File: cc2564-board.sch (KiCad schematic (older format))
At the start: 70 parts, among them J1 TYPE-C-31-M-12, J2 Conn_ARM_JTAG_SWD_10, J3 Conn_01x16, J4 Conn_01x16, J5 BOOT, J7 1909763-1, J8 Conn_01x04, SW1 SW_Push, U1 LD1117#33, U2 USBLC6-2P6, U3 LD1117#18, U4 STM32F103C8Tx, U5 TXB0104D, U6 TXB0104D, U7 CC2564CRVMR, Y1 ECS-80-18-30-JGN-TR, Y2 ECS-327MVATX-3-CN-TR, Y3 ECS-260-8-36CKM-TR

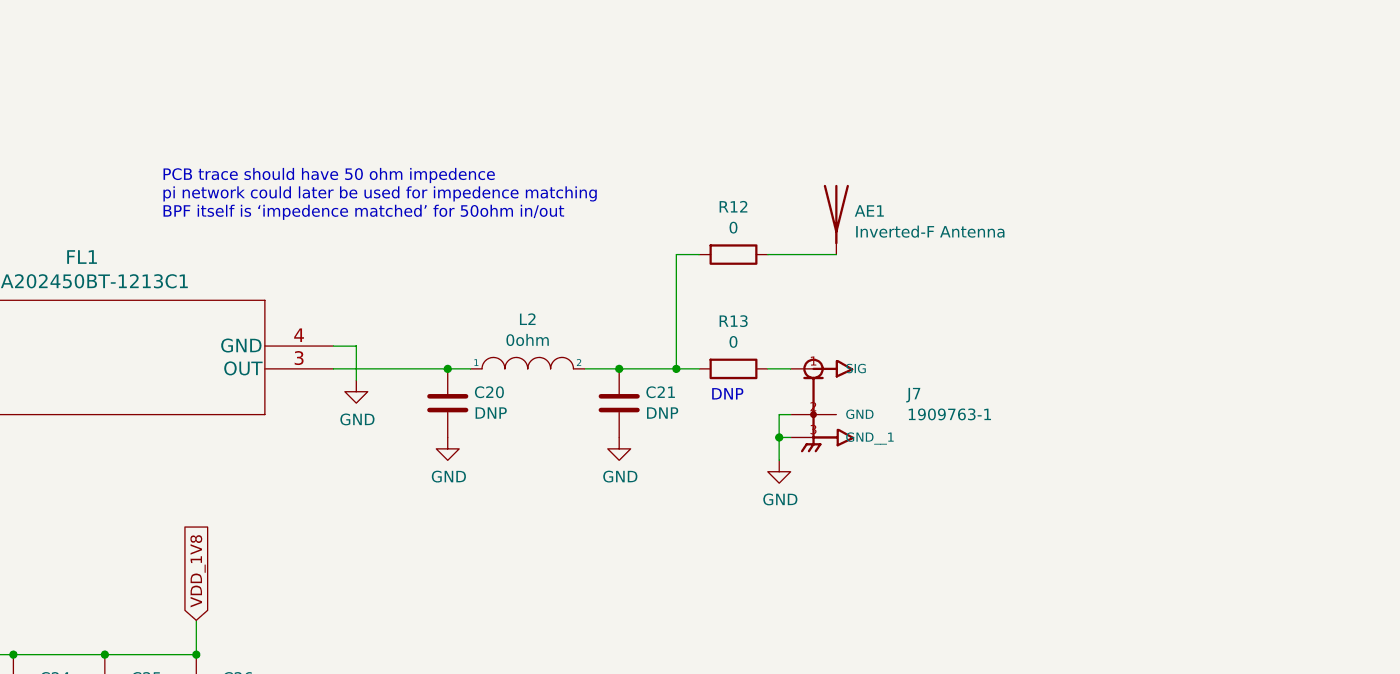
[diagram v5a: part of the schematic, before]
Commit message: Use meandered PIFA from TI app note AN043
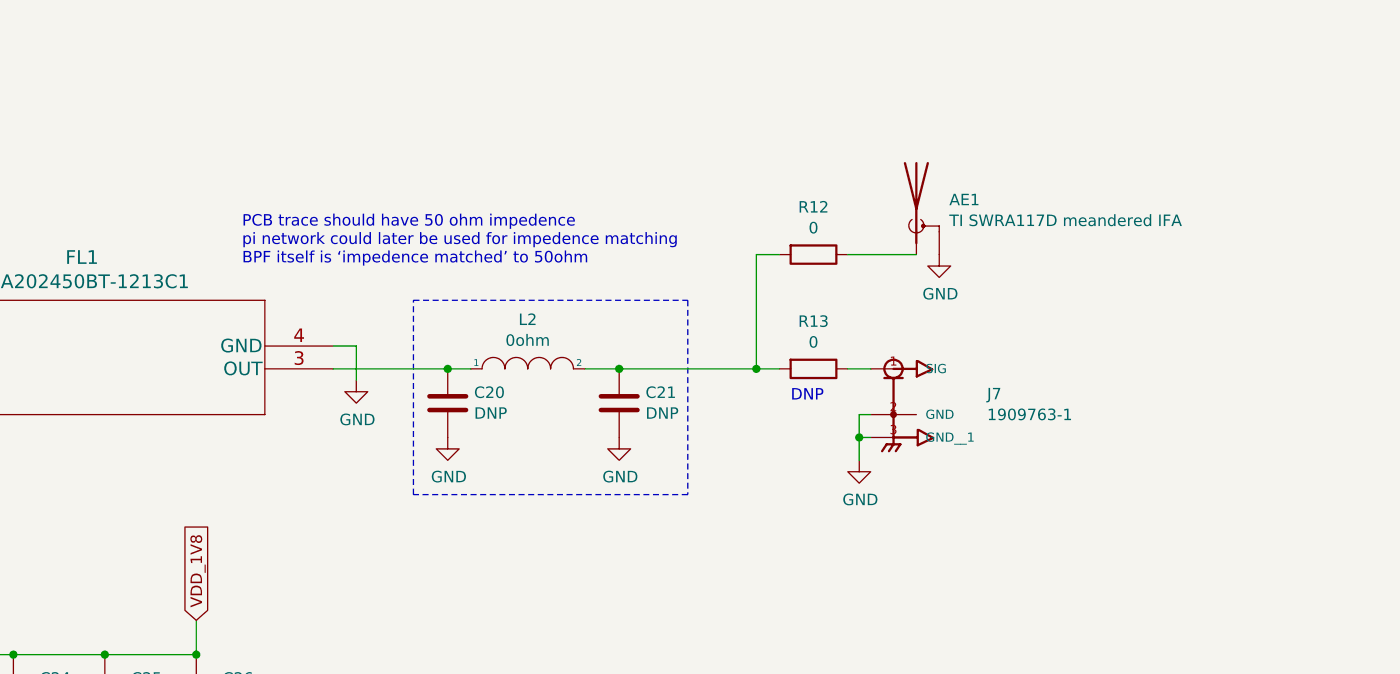
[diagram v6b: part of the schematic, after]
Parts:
- removed AE1: Inverted-F Antenna, symbol Device:Antenna
- added AE1: TI SWRA117D meandered IFA, RF_Antenna:Texas_SWRA117D_2.4GHz_Right, symbol Device:Antenna_Shield
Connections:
- net GND: now also AE1.2 (Shield)
- net at R12.1: now also AE1.1 (A)
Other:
- note added: "PCB trace should have 50 ohm impedence\npi network could later be used for impedence matching\nBPF itself is ‘impedence matched’ to 50ohm"
- note removed: "PCB trace should have 50 ohm impedence\npi network could later be used for impedence matching\nBPF itself is ‘impedence matched’ for 50ohm in/out"
- moved on the sheet: J7, R12, R13
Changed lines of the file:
@@
 L power:GND #PWR029
 U 1 1 60FF41DF
-P 11350 9450
-F 0 "#PWR029" H 11350 9200 50  0001 C CNN
-F 1 "GND" H 11355 9277 50  0000 C CNN
-F 2 "" H 11350 9450 50  0001 C CNN
-F 3 "" H 11350 9450 50  0001 C CNN
-	1    11350 9450
+P 11700 9450
+F 0 "#PWR029" H 11700 9200 50  0001 C CNN
+F 1 "GND" H 11705 9277 50  0000 C CNN
+F 2 "" H 11700 9450 50  0001 C CNN
+F 3 "" H 11700 9450 50  0001 C CNN
+	1    11700 9450
 	1    0    0    -1
 $EndComp
@@
 NSHUTDOWN_1V8
 Wire Wire Line
-	11300 9050 11400 9050
-Text Notes 11050 9200 0    50   ~ 0
+	11650 9050 11750 9050
+Text Notes 11400 9200 0    50   ~ 0
 DNP
 $Comp
 L Device:R R13
 U 1 1 60FF5CB5
-P 11150 9050
-F 0 "R13" V 10943 9050 50  0000 C CNN
-F 1 "0" V 11034 9050 50  0000 C CNN
-F 2 "Resistor_SMD:R_0402_1005Metric_Pad0.72x0.64mm_HandSolder" V 11080 9050 50  0001 C CNN
-F 3 "~" H 11150 9050 50  0001 C CNN
-	1    11150 9050
+P 11500 9050
+F 0 "R13" V 11293 9050 50  0000 C CNN
+F 1 "0" V 11384 9050 50  0000 C CNN
+F 2 "Resistor_SMD:R_0402_1005Metric_Pad0.72x0.64mm_HandSolder" V 11430 9050 50  0001 C CNN
+F 3 "~" H 11500 9050 50  0001 C CNN
+	1    11500 9050
 	0    1    1    0
-$EndComp
-$Comp
-L Device:Antenna AE1
-U 1 1 610FD073
-P 11600 8350
-F 0 "AE1" H 11680 8339 50  0000 L CNN
-F 1 "Inverted-F Antenna" H 11680 8248 50  0000 L CNN
-F 2 "" H 11600 8350 50  0001 C CNN
-F 3 "~" H 11600 8350 50  0001 C CNN
-	1    11600 8350
-	1    0    0    -1
 $EndComp
 $Comp
@@
 L Device:R R12
 U 1 1 61154716
-P 11150 8550
-F 0 "R12" V 10943 8550 50  0000 C CNN
-F 1 "0" V 11034 8550 50  0000 C CNN
-F 2 "Resistor_SMD:R_0402_1005Metric_Pad0.72x0.64mm_HandSolder" V 11080 8550 50  0001 C CNN
-F 3 "~" H 11150 8550 50  0001 C CNN
-	1    11150 8550
+P 11500 8550
+F 0 "R12" V 11293 8550 50  0000 C CNN
+F 1 "0" V 11384 8550 50  0000 C CNN
+F 2 "Resistor_SMD:R_0402_1005Metric_Pad0.72x0.64mm_HandSolder" V 11430 8550 50  0001 C CNN
+F 3 "~" H 11500 8550 50  0001 C CNN
+	1    11500 8550
 	0    1    1    0
 $EndComp
 Wire Wire Line
-	10900 9050 10900 8550
-Wire Wire Line
-	10900 8550 11000 8550
-Connection ~ 10900 9050
-Wire Wire Line
-	10900 9050 11000 9050
-Wire Wire Line
-	11300 8550 11600 8550
+	11250 9050 11250 8550
+Wire Wire Line
+	11250 8550 11350 8550
+Connection ~ 11250 9050
+Wire Wire Line
+	11250 9050 11350 9050
+Wire Wire Line
+	11650 8550 11950 8550
 $Comp
 L power:GND #PWR027
@@
 	1    0    0    -1
 $EndComp
-Text Notes 8650 8400 0    50   ~ 0
-PCB trace should have 50 ohm impedence\npi network could later be used for impedence matching\nBPF itself is ‘impedence matched’ for 50ohm in/out
+Text Notes 9000 8600 0    50   ~ 0
+PCB trace should have 50 ohm impedence\npi network could later be used for impedence matching\nBPF itself is ‘impedence matched’ to 50ohm
 $Comp
 L Device:C C22
@@
 Wire Wire Line
 	9900 9050 10000 9050
-Connection ~ 10650 9050
-Wire Wire Line
-	10650 9050 10900 9050
 Wire Wire Line
 	9400 9050 9900 9050
@@
 L UFL-CONNECTOR:1909763-1 J7
 U 1 1 61592833
-P 11500 9150
-F 0 "J7" H 11909 9140 50  0000 L CNN
-F 1 "1909763-1" H 11909 9049 50  0000 L CNN
-F 2 "cc2654-board-footprints:UFL-TE_1909763-1" H 11500 9150 50  0001 L BNN
-F 3 "" H 11500 9150 50  0001 L BNN
-F 4 "1909763-1" H 11500 9150 50  0001 L BNN "Comment"
-F 5 "1" H 11500 9150 50  0001 L BNN "Number_of_Positions"
-	1    11500 9150
-	1    0    0    -1
-$EndComp
-Wire Wire Line
-	11400 9250 11350 9250
-Wire Wire Line
-	11350 9250 11350 9350
-Wire Wire Line
-	11400 9350 11350 9350
-Connection ~ 11350 9350
-Wire Wire Line
-	11350 9350 11350 9450
+P 11850 9150
+F 0 "J7" H 12259 9140 50  0000 L CNN
+F 1 "1909763-1" H 12259 9049 50  0000 L CNN
+F 2 "cc2654-board-footprints:UFL-TE_1909763-1" H 11850 9150 50  0001 L BNN
+F 3 "" H 11850 9150 50  0001 L BNN
+F 4 "1909763-1" H 11850 9150 50  0001 L BNN "Comment"
+F 5 "1" H 11850 9150 50  0001 L BNN "Number_of_Positions"
+	1    11850 9150
+	1    0    0    -1
+$EndComp
+Wire Wire Line
+	11750 9250 11700 9250
+Wire Wire Line
+	11700 9250 11700 9350
+Wire Wire Line
+	11750 9350 11700 9350
+Connection ~ 11700 9350
+Wire Wire Line
+	11700 9350 11700 9450
 $Comp
 L DEA202450BT-1213C1:DEA202450BT-1213C1 FL1
@@
 	1650 6500 1650 6450
 Connection ~ 1650 6450
+Wire Wire Line
+	10650 9050 11250 9050
+Connection ~ 10650 9050
+Wire Notes Line
+	9750 9600 9750 8750
+Wire Notes Line
+	9750 8750 10950 8750
+Wire Notes Line
+	10950 8750 10950 9600
+Wire Notes Line
+	10950 9600 9750 9600
+$Comp
+L Device:Antenna_Shield AE1
+U 1 1 61810854
+P 11950 8350
+F 0 "AE1" H 12094 8389 50  0000 L CNN
+F 1 "TI SWRA117D meandered IFA" H 12094 8298 50  0000 L CNN
+F 2 "RF_Antenna:Texas_SWRA117D_2.4GHz_Right" H 11950 8450 50  0001 C CNN
+F 3 "~" H 11950 8450 50  0001 C CNN
+	1    11950 8350
+	1    0    0    -1
+$EndComp
+$Comp
+L power:GND #PWR0102
+U 1 1 61816E28
+P 12050 8550
+F 0 "#PWR0102" H 12050 8300 50  0001 C CNN
+F 1 "GND" H 12055 8377 50  0000 C CNN
+F 2 "" H 12050 8550 50  0001 C CNN
+F 3 "" H 12050 8550 50  0001 C CNN
+	1    12050 8550
+	1    0    0    -1
+$EndComp
 $EndSCHEMATC

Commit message: More footprint updates
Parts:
- C1, C10, C11, C12, C13, C14, C15, C16, C17, C18, C19, C2, C20, C21, C22, C23, C24, C25, C26, C27, C28, C3, C4, C5, C6, C7, C8, C9: footprint Capacitor_SMD:C_0603_1608Metric_Pad1.08x0.95mm_HandSolder -> Capacitor_SMD:C_0402_1005Metric_Pad0.74x0.62mm_HandSolder
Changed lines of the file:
@@
 F 0 "C23" H 7765 10496 50  0000 L CNN
 F 1 "0.1uF" H 7765 10405 50  0000 L CNN
-F 2 "Capacitor_SMD:C_0603_1608Metric_Pad1.08x0.95mm_HandSolder" H 7688 10300 50  0001 C CNN
+F 2 "Capacitor_SMD:C_0402_1005Metric_Pad0.74x0.62mm_HandSolder" H 7688 10300 50  0001 C CNN
 F 3 "~" H 7650 10450 50  0001 C CNN
 	1    7650 10450
@@
 F 0 "C24" H 8115 10496 50  0000 L CNN
 F 1 "0.1uF" H 8115 10405 50  0000 L CNN
-F 2 "Capacitor_SMD:C_0603_1608Metric_Pad1.08x0.95mm_HandSolder" H 8038 10300 50  0001 C CNN
+F 2 "Capacitor_SMD:C_0402_1005Metric_Pad0.74x0.62mm_HandSolder" H 8038 10300 50  0001 C CNN
 F 3 "~" H 8000 10450 50  0001 C CNN
 	1    8000 10450
@@
 F 0 "C25" H 8515 10496 50  0000 L CNN
 F 1 "0.1uF" H 8515 10405 50  0000 L CNN
-F 2 "Capacitor_SMD:C_0603_1608Metric_Pad1.08x0.95mm_HandSolder" H 8438 10300 50  0001 C CNN
+F 2 "Capacitor_SMD:C_0402_1005Metric_Pad0.74x0.62mm_HandSolder" H 8438 10300 50  0001 C CNN
 F 3 "~" H 8400 10450 50  0001 C CNN
 	1    8400 10450
@@
 F 0 "C26" H 8915 10496 50  0000 L CNN
 F 1 "0.1uF" H 8915 10405 50  0000 L CNN
-F 2 "Capacitor_SMD:C_0603_1608Metric_Pad1.08x0.95mm_HandSolder" H 8838 10300 50  0001 C CNN
+F 2 "Capacitor_SMD:C_0402_1005Metric_Pad0.74x0.62mm_HandSolder" H 8838 10300 50  0001 C CNN
 F 3 "~" H 8800 10450 50  0001 C CNN
 	1    8800 10450
@@
 F 0 "C3" H 12015 2046 50  0000 L CNN
 F 1 "100nF" H 12015 1955 50  0000 L CNN
-F 2 "Capacitor_SMD:C_0603_1608Metric_Pad1.08x0.95mm_HandSolder" H 11938 1850 50  0001 C CNN
+F 2 "Capacitor_SMD:C_0402_1005Metric_Pad0.74x0.62mm_HandSolder" H 11938 1850 50  0001 C CNN
 F 3 "~" H 11900 2000 50  0001 C CNN
 	1    11900 2000
@@
 F 0 "C4" H 12465 2046 50  0000 L CNN
 F 1 "100nF" H 12465 1955 50  0000 L CNN
-F 2 "Capacitor_SMD:C_0603_1608Metric_Pad1.08x0.95mm_HandSolder" H 12388 1850 50  0001 C CNN
+F 2 "Capacitor_SMD:C_0402_1005Metric_Pad0.74x0.62mm_HandSolder" H 12388 1850 50  0001 C CNN
 F 3 "~" H 12350 2000 50  0001 C CNN
 	1    12350 2000
@@
 F 0 "C5" H 12965 2046 50  0000 L CNN
 F 1 "100nF" H 12965 1955 50  0000 L CNN
-F 2 "Capacitor_SMD:C_0603_1608Metric_Pad1.08x0.95mm_HandSolder" H 12888 1850 50  0001 C CNN
+F 2 "Capacitor_SMD:C_0402_1005Metric_Pad0.74x0.62mm_HandSolder" H 12888 1850 50  0001 C CNN
 F 3 "~" H 12850 2000 50  0001 C CNN
 	1    12850 2000
@@
 F 0 "C6" H 13415 2046 50  0000 L CNN
 F 1 "100nF" H 13415 1955 50  0000 L CNN
-F 2 "Capacitor_SMD:C_0603_1608Metric_Pad1.08x0.95mm_HandSolder" H 13338 1850 50  0001 C CNN
+F 2 "Capacitor_SMD:C_0402_1005Metric_Pad0.74x0.62mm_HandSolder" H 13338 1850 50  0001 C CNN
 F 3 "~" H 13300 2000 50  0001 C CNN
 	1    13300 2000
@@
 F 0 "C7" H 13815 2046 50  0000 L CNN
 F 1 "10uF" H 13815 1955 50  0000 L CNN
-F 2 "Capacitor_SMD:C_0603_1608Metric_Pad1.08x0.95mm_HandSolder" H 13738 1850 50  0001 C CNN
+F 2 "Capacitor_SMD:C_0402_1005Metric_Pad0.74x0.62mm_HandSolder" H 13738 1850 50  0001 C CNN
 F 3 "~" H 13700 2000 50  0001 C CNN
 	1    13700 2000
@@
 F 0 "C9" H 15815 2096 50  0000 L CNN
 F 1 "1uF" H 15815 2005 50  0000 L CNN
-F 2 "Capacitor_SMD:C_0603_1608Metric_Pad1.08x0.95mm_HandSolder" H 15738 1900 50  0001 C CNN
+F 2 "Capacitor_SMD:C_0402_1005Metric_Pad0.74x0.62mm_HandSolder" H 15738 1900 50  0001 C CNN
 F 3 "~" H 15700 2050 50  0001 C CNN
 	1    15700 2050
@@
 F 0 "C13" H 2415 3796 50  0000 L CNN
 F 1 "100nF" H 2415 3705 50  0000 L CNN
-F 2 "Capacitor_SMD:C_0603_1608Metric_Pad1.08x0.95mm_HandSolder" H 2338 3600 50  0001 C CNN
+F 2 "Capacitor_SMD:C_0402_1005Metric_Pad0.74x0.62mm_HandSolder" H 2338 3600 50  0001 C CNN
 F 3 "~" H 2300 3750 50  0001 C CNN
 	1    2300 3750
@@
 F 0 "C1" H 7115 1696 50  0000 L CNN
 F 1 "100nF" H 7115 1605 50  0000 L CNN
-F 2 "Capacitor_SMD:C_0603_1608Metric_Pad1.08x0.95mm_HandSolder" H 7038 1500 50  0001 C CNN
+F 2 "Capacitor_SMD:C_0402_1005Metric_Pad0.74x0.62mm_HandSolder" H 7038 1500 50  0001 C CNN
 F 3 "~" H 7000 1650 50  0001 C CNN
 	1    7000 1650
@@
 F 0 "C2" H 8115 1696 50  0000 L CNN
 F 1 "10uF" H 8115 1605 50  0000 L CNN
-F 2 "Capacitor_SMD:C_0603_1608Metric_Pad1.08x0.95mm_HandSolder" H 8038 1500 50  0001 C CNN
+F 2 "Capacitor_SMD:C_0402_1005Metric_Pad0.74x0.62mm_HandSolder" H 8038 1500 50  0001 C CNN
 F 3 "~" H 8000 1650 50  0001 C CNN
 	1    8000 1650
@@
 F 0 "C11" H 7115 2646 50  0000 L CNN
 F 1 "100nF" H 7115 2555 50  0000 L CNN
-F 2 "Capacitor_SMD:C_0603_1608Metric_Pad1.08x0.95mm_HandSolder" H 7038 2450 50  0001 C CNN
+F 2 "Capacitor_SMD:C_0402_1005Metric_Pad0.74x0.62mm_HandSolder" H 7038 2450 50  0001 C CNN
 F 3 "~" H 7000 2600 50  0001 C CNN
 	1    7000 2600
@@
 F 0 "C12" H 8165 2646 50  0000 L CNN
 F 1 "10uF" H 8165 2555 50  0000 L CNN
-F 2 "Capacitor_SMD:C_0603_1608Metric_Pad1.08x0.95mm_HandSolder" H 8088 2450 50  0001 C CNN
+F 2 "Capacitor_SMD:C_0402_1005Metric_Pad0.74x0.62mm_HandSolder" H 8088 2450 50  0001 C CNN
 F 3 "~" H 8050 2600 50  0001 C CNN
 	1    8050 2600
@@
 F 0 "C16" H 7715 4446 50  0000 L CNN
 F 1 "0.1uF" H 7715 4355 50  0000 L CNN
-F 2 "Capacitor_SMD:C_0603_1608Metric_Pad1.08x0.95mm_HandSolder" H 7638 4250 50  0001 C CNN
+F 2 "Capacitor_SMD:C_0402_1005Metric_Pad0.74x0.62mm_HandSolder" H 7638 4250 50  0001 C CNN
 F 3 "~" H 7600 4400 50  0001 C CNN
 	1    7600 4400
@@
 F 0 "C17" H 8915 4446 50  0000 L CNN
 F 1 "0.1uF" H 8915 4355 50  0000 L CNN
-F 2 "Capacitor_SMD:C_0603_1608Metric_Pad1.08x0.95mm_HandSolder" H 8838 4250 50  0001 C CNN
+F 2 "Capacitor_SMD:C_0402_1005Metric_Pad0.74x0.62mm_HandSolder" H 8838 4250 50  0001 C CNN
 F 3 "~" H 8800 4400 50  0001 C CNN
 	1    8800 4400
@@
 F 0 "C27" V 2800 13000 50  0000 L CNN
 F 1 "10 pF" V 2500 12950 50  0000 L CNN
-F 2 "Capacitor_SMD:C_0603_1608Metric_Pad1.08x0.95mm_HandSolder" H 2688 12900 50  0001 C CNN
+F 2 "Capacitor_SMD:C_0402_1005Metric_Pad0.74x0.62mm_HandSolder" H 2688 12900 50  0001 C CNN
 F 3 "~" H 2650 13050 50  0001 C CNN
 	1    2650 13050
@@
 F 0 "C28" V 3550 13000 50  0000 L CNN
 F 1 "10 pF" V 3250 12950 50  0000 L CNN
-F 2 "Capacitor_SMD:C_0603_1608Metric_Pad1.08x0.95mm_HandSolder" H 3438 12900 50  0001 C CNN
+F 2 "Capacitor_SMD:C_0402_1005Metric_Pad0.74x0.62mm_HandSolder" H 3438 12900 50  0001 C CNN
 F 3 "~" H 3400 13050 50  0001 C CNN
 	1    3400 13050
@@
 F 0 "C19" V 2550 4800 50  0000 L CNN
 F 1 "20 pF" V 2250 4750 50  0000 L CNN
-F 2 "Capacitor_SMD:C_0603_1608Metric_Pad1.08x0.95mm_HandSolder" H 2438 4700 50  0001 C CNN
+F 2 "Capacitor_SMD:C_0402_1005Metric_Pad0.74x0.62mm_HandSolder" H 2438 4700 50  0001 C CNN
 F 3 "~" H 2400 4850 50  0001 C CNN
 	1    2400 4850
@@
 F 0 "C8" H 15365 2096 50  0000 L CNN
 F 1 "100nF" H 15365 2005 50  0000 L CNN
-F 2 "Capacitor_SMD:C_0603_1608Metric_Pad1.08x0.95mm_HandSolder" H 15288 1900 50  0001 C CNN
+F 2 "Capacitor_SMD:C_0402_1005Metric_Pad0.74x0.62mm_HandSolder" H 15288 1900 50  0001 C CNN
 F 3 "~" H 15250 2050 50  0001 C CNN
 	1    15250 2050
@@
 F 0 "C10" H 17615 2096 50  0000 L CNN
 F 1 "0.1uF" H 17615 2005 50  0000 L CNN
-F 2 "Capacitor_SMD:C_0603_1608Metric_Pad1.08x0.95mm_HandSolder" H 17538 1900 50  0001 C CNN
+F 2 "Capacitor_SMD:C_0402_1005Metric_Pad0.74x0.62mm_HandSolder" H 17538 1900 50  0001 C CNN
 F 3 "~" H 17500 2050 50  0001 C CNN
 	1    17500 2050
@@
 F 0 "C14" H 10915 4396 50  0000 L CNN
 F 1 "0.1uF" H 10915 4305 50  0000 L CNN
-F 2 "Capacitor_SMD:C_0603_1608Metric_Pad1.08x0.95mm_HandSolder" H 10838 4200 50  0001 C CNN
+F 2 "Capacitor_SMD:C_0402_1005Metric_Pad0.74x0.62mm_HandSolder" H 10838 4200 50  0001 C CNN
 F 3 "~" H 10800 4350 50  0001 C CNN
 	1    10800 4350
@@
 F 0 "C15" H 12115 4396 50  0000 L CNN
 F 1 "0.1uF" H 12115 4305 50  0000 L CNN
-F 2 "Capacitor_SMD:C_0603_1608Metric_Pad1.08x0.95mm_HandSolder" H 12038 4200 50  0001 C CNN
+F 2 "Capacitor_SMD:C_0402_1005Metric_Pad0.74x0.62mm_HandSolder" H 12038 4200 50  0001 C CNN
 F 3 "~" H 12000 4350 50  0001 C CNN
 	1    12000 4350
@@
 F 0 "C20" H 10015 9246 50  0000 L CNN
 F 1 "DNP" H 10015 9155 50  0000 L CNN
-F 2 "Capacitor_SMD:C_0603_1608Metric_Pad1.08x0.95mm_HandSolder" H 9938 9050 50  0001 C CNN
+F 2 "Capacitor_SMD:C_0402_1005Metric_Pad0.74x0.62mm_HandSolder" H 9938 9050 50  0001 C CNN
 F 3 "~" H 9900 9200 50  0001 C CNN
 	1    9900 9200
@@
 F 0 "C21" H 10765 9246 50  0000 L CNN
 F 1 "DNP" H 10765 9155 50  0000 L CNN
-F 2 "Capacitor_SMD:C_0603_1608Metric_Pad1.08x0.95mm_HandSolder" H 10688 9050 50  0001 C CNN
+F 2 "Capacitor_SMD:C_0402_1005Metric_Pad0.74x0.62mm_HandSolder" H 10688 9050 50  0001 C CNN
 F 3 "~" H 10650 9200 50  0001 C CNN
 	1    10650 9200
@@
 F 0 "C22" H 7215 9546 50  0000 L CNN
 F 1 "22pF" H 7215 9455 50  0000 L CNN
-F 2 "Capacitor_SMD:C_0603_1608Metric_Pad1.08x0.95mm_HandSolder" H 7138 9350 50  0001 C CNN
+F 2 "Capacitor_SMD:C_0402_1005Metric_Pad0.74x0.62mm_HandSolder" H 7138 9350 50  0001 C CNN
 F 3 "~" H 7100 9500 50  0001 C CNN
 	1    7100 9500
@@
 F 0 "C18" V 2000 4800 50  0000 L CNN
 F 1 "20 pF" V 1700 4750 50  0000 L CNN
-F 2 "Capacitor_SMD:C_0603_1608Metric_Pad1.08x0.95mm_HandSolder" H 1888 4700 50  0001 C CNN
+F 2 "Capacitor_SMD:C_0402_1005Metric_Pad0.74x0.62mm_HandSolder" H 1888 4700 50  0001 C CNN
 F 3 "~" H 1850 4850 50  0001 C CNN
 	1    1850 4850

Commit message: Specify high-Q DC blocking cap
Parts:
- added R10, R4: 10k, Resistor_SMD:R_0402_1005Metric_Pad0.72x0.64mm_HandSolder, symbol Device:R
- C1, C11, C13, C3, C4, C5, C6, C8: value 100nF -> 0.1uF
- renumbered J7 to J6, J8 to J7, R9 to R11, R10 to R12, R11 to R13, R12 to R14, R13 to R15, R14 to R16, R15 to R17, R4 to R5, R5 to R6, R6 to R7, R7 to R8, R8 to R9
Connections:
- net BOOT0: now also R4.2; no longer U4.44 (BOOT0)
- net BOOT1: now also R10.2; no longer U4.20 (PB2)
- new net: R10.1, U4.20 (PB2)
- new net: R4.1, U4.44 (BOOT0)
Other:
- note added: "DC blocking\nrequired for CC2564\nhigh-Q, 25V\ne.g. GRM0225C1E220JA02L"
- note removed: "DC blocking\nrequired for CC2564\nblock 5th harmonic?\n"
- moved on the sheet: C18, C19, C7, R_EXT1, Y1
